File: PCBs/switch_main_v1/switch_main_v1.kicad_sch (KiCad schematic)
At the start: 0 parts

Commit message: Schematic progress
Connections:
- no-connect marks 0 -> 1
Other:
- sheet MCU ports: added ETH_PPS_OUT, MCO1, RMII, SMI; removed none
- sheet PHY 1 ports: added CLK_IN, CLK_OUT, ETHERNET, RGMII, SMI; removed none
- sheet PHY 2 ports: added CLK_IN, CLK_OUT, ETHERNET, RGMII, SMI; removed none
- sheet PHY 3 ports: added CLK_IN, CLK_OUT, ETHERNET, RGMII, SMI; removed none
- sheet PHY 4 ports: added CLK_IN, CLK_OUT, ETHERNET, RGMII, SMI; removed none
- sheet RJ45s ports: added ETHERNET_1, ETHERNET_2, ETHERNET_3, ETHERNET_4; removed none
- sheet Switch ports: added CLK_IN, CLK_OUT, PTP_CLK, RGMII_0, RGMII_1, RGMII_2, RGMII_3, RMII, RST, SPI; removed none
- note added: "Circuits & ICs"
- note added: "Interfaces"
- note added: "Power"
- note added: "Processing"

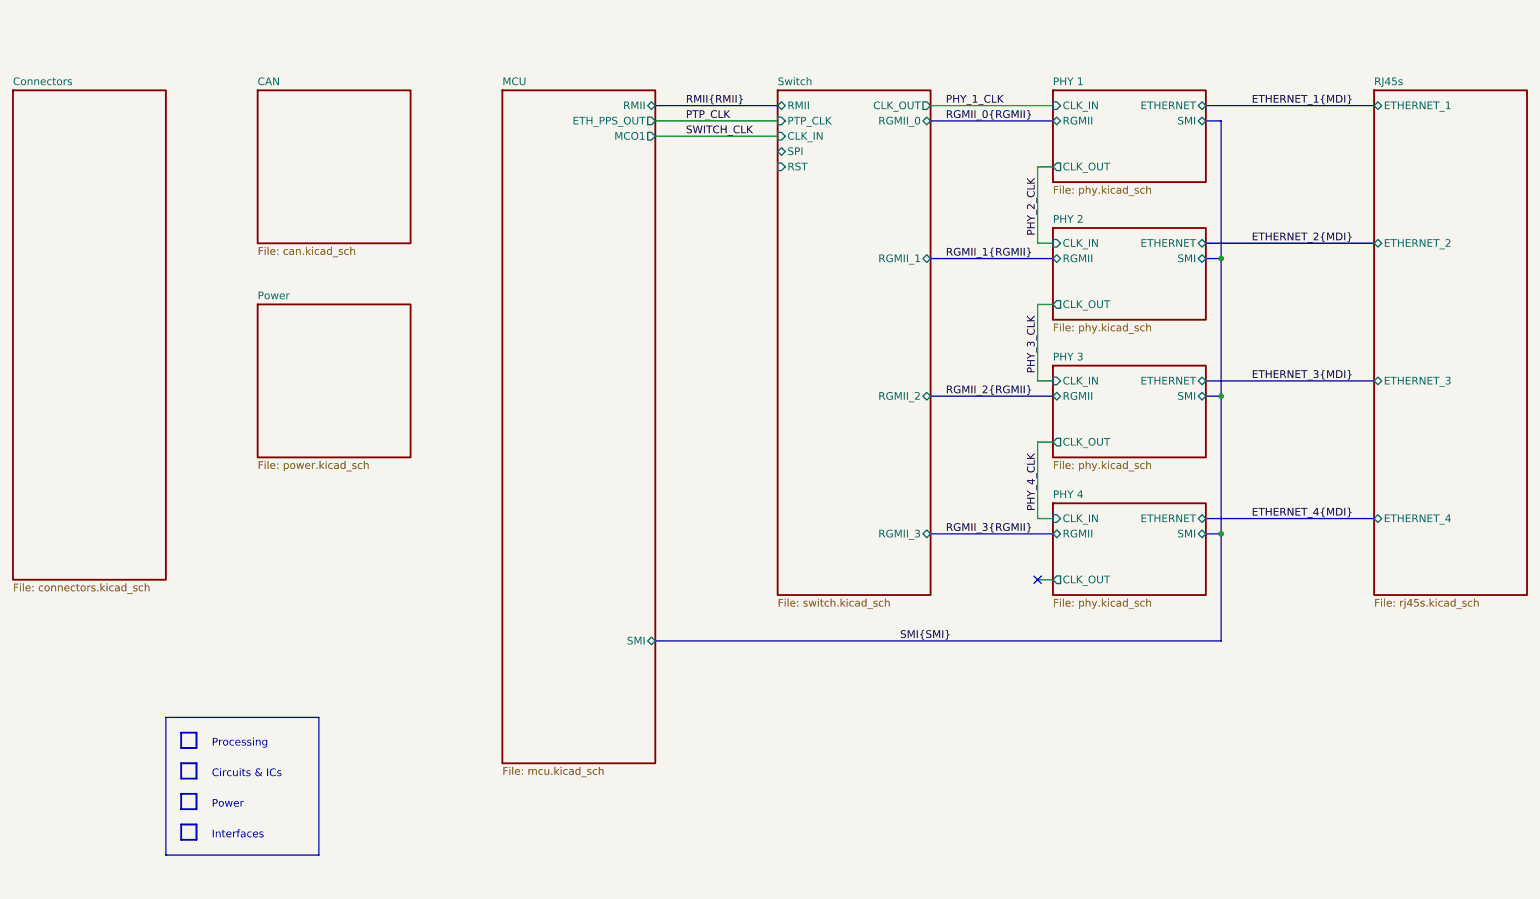
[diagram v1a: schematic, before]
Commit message: Block diagram layout change
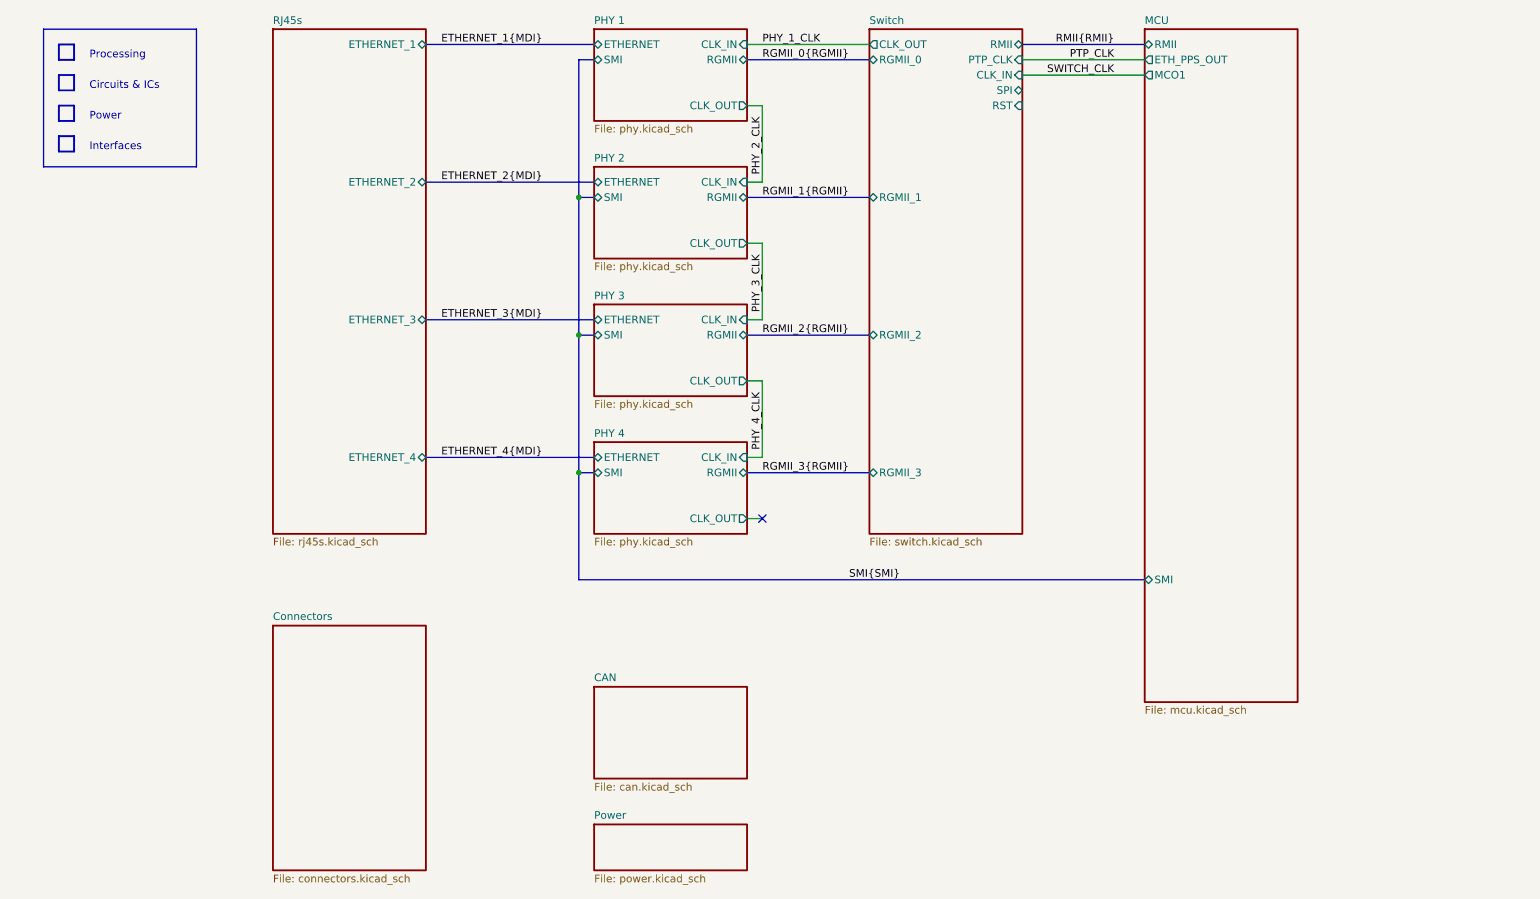
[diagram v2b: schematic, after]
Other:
- company: (none) -> Ben Smith
- title: (none) -> GbE TSN Switch Block Diagram

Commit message: GbE part of schematic done
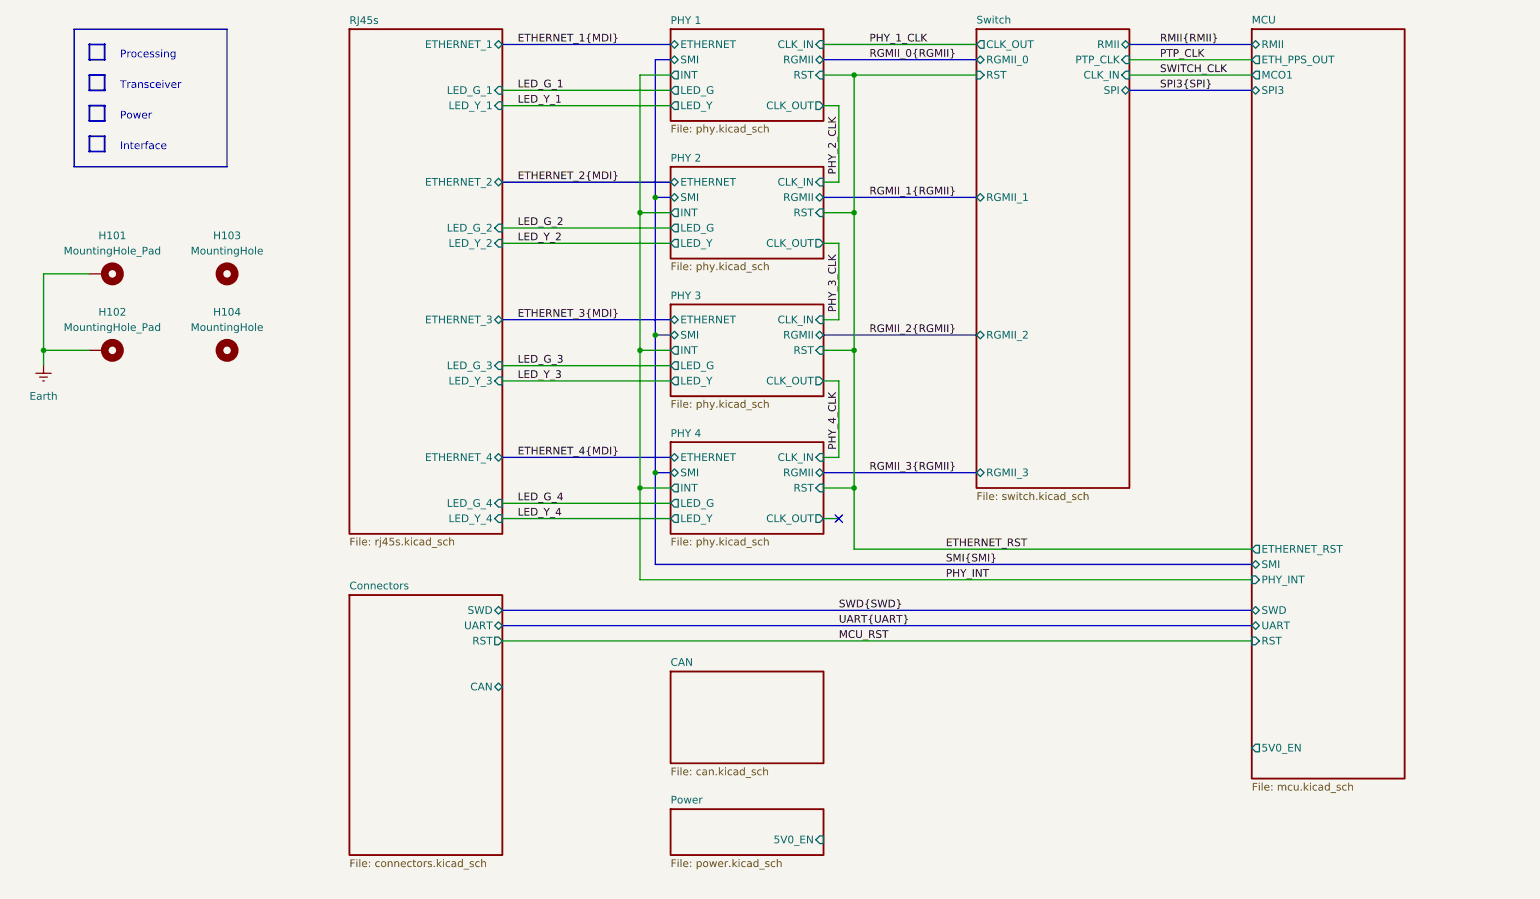
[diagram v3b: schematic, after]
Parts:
- added H101, H102: MountingHole_Pad, MountingHole:MountingHole_3.2mm_M3_DIN965_Pad_TopBottom, symbol Mechanical:MountingHole_Pad
- added H103, H104: MountingHole, MountingHole:MountingHole_3.2mm_M3_DIN965, symbol Mechanical:MountingHole
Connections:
- new net Earth: H101.1, H102.1
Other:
- sheet Connectors ports: added CAN, RST, SWD, UART; removed none
- sheet MCU ports: added 5V0_EN, ETHERNET_RST, PHY_INT, RST, SPI3, SWD, UART; removed none
- sheet PHY 1 ports: added INT, LED_G, LED_Y, RST; removed none
- sheet PHY 2 ports: added INT, LED_G, LED_Y, RST; removed none
- sheet PHY 3 ports: added INT, LED_G, LED_Y, RST; removed none
- sheet PHY 4 ports: added INT, LED_G, LED_Y, RST; removed none
- sheet Power ports: added 5V0_EN; removed none
- sheet RJ45s ports: added LED_G_1, LED_G_2, LED_G_3, LED_G_4, LED_Y_1, LED_Y_2, LED_Y_3, LED_Y_4; removed none
- note added: "Interface"
- note added: "Transceiver"
- note removed: "Circuits & ICs"
- note removed: "Interfaces"

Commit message: Progress on CAN schematic sheet
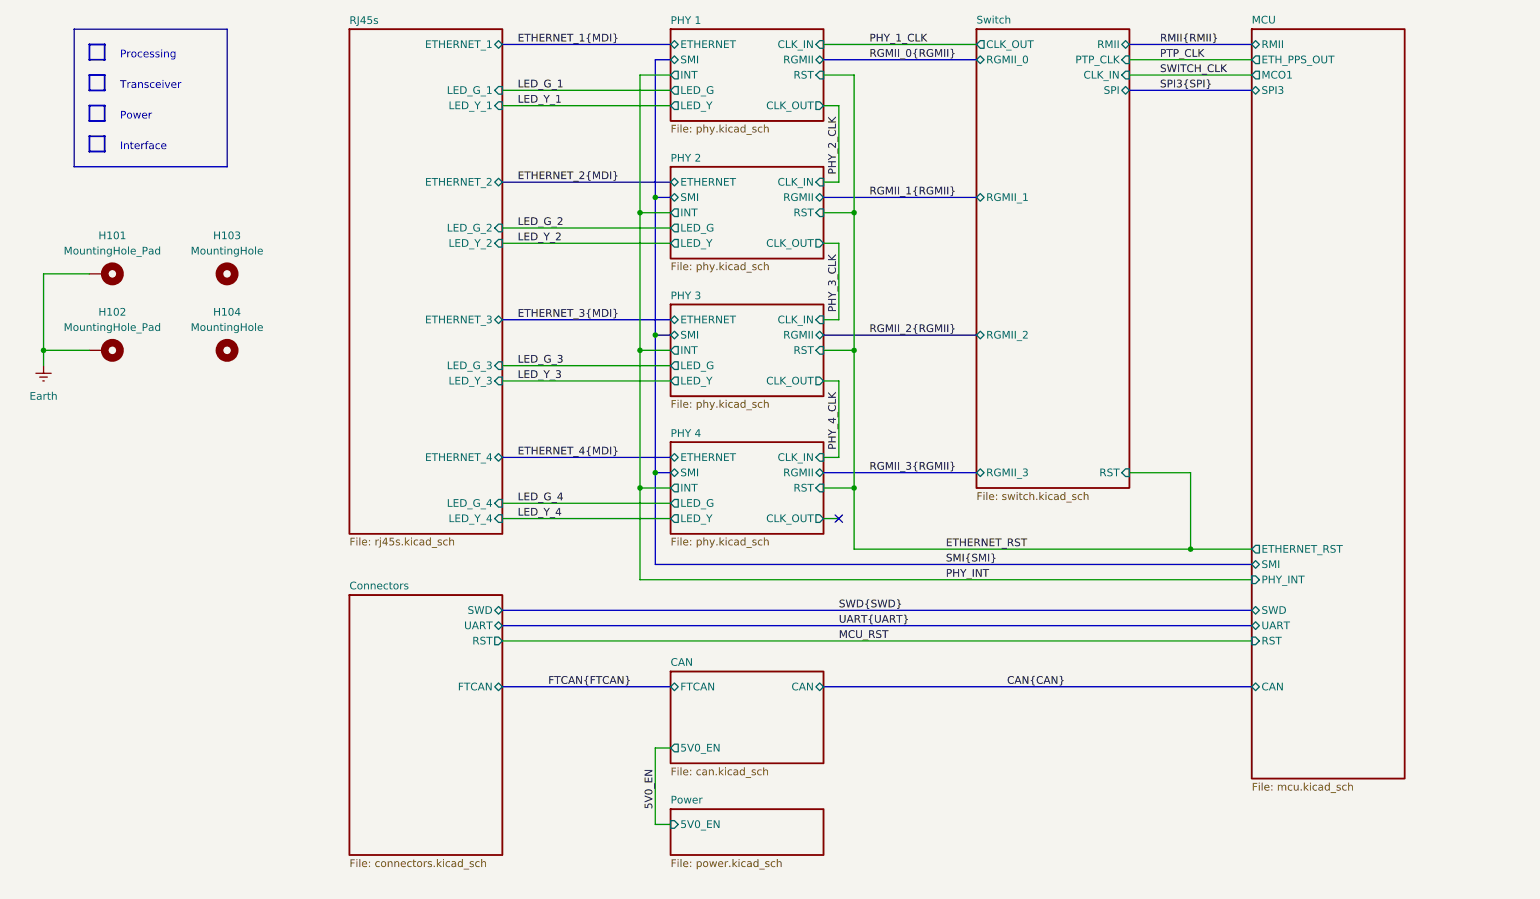
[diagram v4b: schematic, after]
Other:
- sheet CAN ports: added 5V0_EN, CAN, FTCAN; removed none
- sheet Connectors ports: added FTCAN; removed CAN
- sheet MCU ports: added CAN; removed 5V0_EN
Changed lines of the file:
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@@
+	)
+	(junction
+		(at 218.44 114.3)
+		(diameter 0)
+		(color 0 0 0 0)
 	)
 	(junction
@@
 	)
 	(junction
-		(at 162.56 35.56)
-		(diameter 0)
-		(color 0 0 0 0)
-	)
-	(junction
 		(at 162.56 104.14)
 		(diameter 0)
@@
 	(wire
 		(pts
+			(xy 218.44 114.3) (xy 162.56 114.3)
+		)
+		(stroke
+			(width 0)
+			(type default)
+		)
+	)
+	(wire
+		(pts
 			(xy 160.02 99.06) (xy 157.48 99.06)
 		)
@@
 	(bus
 		(pts
+			(xy 104.14 137.16) (xy 132.08 137.16)
+		)
+		(stroke
+			(width 0)
+			(type default)
+		)
+	)
+	(bus
+		(pts
 			(xy 104.14 53.34) (xy 132.08 53.34)
 		)
@@
 	(wire
 		(pts
+			(xy 129.54 147.32) (xy 129.54 160.02)
+		)
+		(stroke
+			(width 0)
+			(type default)
+		)
+	)
+	(wire
+		(pts
 			(xy 104.14 109.22) (xy 132.08 109.22)
 		)
@@
 	(wire
 		(pts
-			(xy 228.6 114.3) (xy 162.56 114.3)
+			(xy 228.6 114.3) (xy 218.44 114.3)
 		)
 		(stroke
@@
 	(wire
 		(pts
+			(xy 208.28 101.6) (xy 218.44 101.6)
+		)
+		(stroke
+			(width 0)
+			(type default)
+		)
+	)
+	(wire
+		(pts
 			(xy 127 104.14) (xy 127 81.28)
 		)
@@
 	(wire
 		(pts
+			(xy 132.08 160.02) (xy 129.54 160.02)
+		)
+		(stroke
+			(width 0)
+			(type default)
+		)
+	)
+	(wire
+		(pts
 			(xy 160.02 76.2) (xy 157.48 76.2)
 		)
@@
 		)
 	)
+	(bus
+		(pts
+			(xy 157.48 137.16) (xy 228.6 137.16)
+		)
+		(stroke
+			(width 0)
+			(type default)
+		)
+	)
 	(wire
 		(pts
@@
 	(wire
 		(pts
-			(xy 162.56 35.56) (xy 182.88 35.56)
+			(xy 129.54 147.32) (xy 132.08 147.32)
 		)
 		(stroke
@@
 		(pts
 			(xy 157.48 81.28) (xy 162.56 81.28)
+		)
+		(stroke
+			(width 0)
+			(type default)
+		)
+	)
+	(wire
+		(pts
+			(xy 218.44 101.6) (xy 218.44 114.3)
 		)
 		(stroke
@@
 		)
 	)
+	(label "CAN{CAN}"
+		(at 187.96 137.16 0)
+		(fields_autoplaced yes)
+		(effects
+			(font
+				(size 1.27 1.27)
+			)
+			(justify left bottom)
+		)
+	)
 	(label "LED_Y_3"
 		(at 106.68 86.36 0)
@@
 		)
 	)
+	(label "FTCAN{FTCAN}"
+		(at 111.76 137.16 0)
+		(fields_autoplaced yes)
+		(effects
+			(font
+				(size 1.27 1.27)
+			)
+			(justify left bottom)
+		)
+	)
 	(label "SWITCH_CLK"
 		(at 213.36 35.56 0)
@@
 	(label "LED_Y_2"
 		(at 106.68 63.5 0)
+		(fields_autoplaced yes)
+		(effects
+			(font
+				(size 1.27 1.27)
+			)
+			(justify left bottom)
+		)
+	)
+	(label "5V0_EN"
+		(at 129.54 157.48 90)
 		(fields_autoplaced yes)
 		(effects
@@
 		)
 		(pin "RST" input
-			(at 182.88 35.56 180)
-			(effects
-				(font
-					(size 1.27 1.27)
-				)
-				(justify left)
+			(at 208.28 101.6 0)
+			(effects
+				(font
+					(size 1.27 1.27)
+				)
+				(justify right)
 			)
 		)
@@
 			)
 		)
+		(pin "5V0_EN" output
+			(at 132.08 147.32 180)
+			(effects
+				(font
+					(size 1.27 1.27)
+				)
+				(justify left)
+			)
+		)
+		(pin "CAN" bidirectional
+			(at 157.48 137.16 0)
+			(effects
+				(font
+					(size 1.27 1.27)
+				)
+				(justify right)
+			)
+		)
+		(pin "FTCAN" bidirectional
+			(at 132.08 137.16 180)
+			(effects
+				(font
+					(size 1.27 1.27)
+				)
+				(justify left)
+			)
+		)
 		(instances
 			(project "switch_main_v1"
@@
 			)
 		)
-		(pin "CAN" bidirectional
-			(at 104.14 137.16 0)
-			(effects
-				(font
-					(size 1.27 1.27)
-				)
-				(justify right)
-			)
-		)
 		(pin "UART" bidirectional
 			(at 104.14 127 0)
@@
 		(pin "RST" output
 			(at 104.14 129.54 0)
+			(effects
+				(font
+					(size 1.27 1.27)
+				)
+				(justify right)
+			)
+		)
+		(pin "FTCAN" bidirectional
+			(at 104.14 137.16 0)
 			(effects
 				(font
@@
 			)
 		)
-		(pin "5V0_EN" output
-			(at 228.6 147.32 180)
-			(effects
-				(font
-					(size 1.27 1.27)
-				)
-				(justify left)
-			)
-		)
 		(pin "ETHERNET_RST" output
 			(at 228.6 114.3 180)
@@
 		(pin "SWD" bidirectional
 			(at 228.6 124.46 180)
+			(effects
+				(font
+					(size 1.27 1.27)
+				)
+				(justify left)
+			)
+		)
+		(pin "CAN" bidirectional
+			(at 228.6 137.16 180)
 			(effects
 				(font
@@
 		)
 		(pin "5V0_EN" input
-			(at 157.48 162.56 0)
-			(effects
-				(font
-					(size 1.27 1.27)
-				)
-				(justify right)
-			)
-		)
+			(at 132.08 160.02 180)
+			(effects
+				(font
+					(size 1.27 1.27)
+				)
+				(justify left)
+			)
+		)

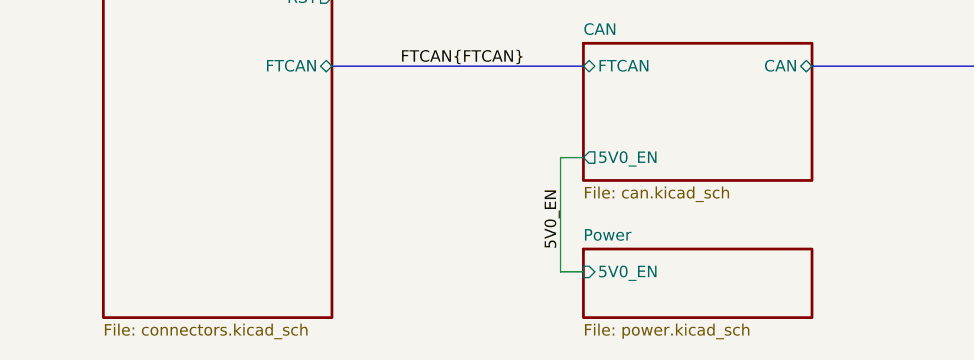
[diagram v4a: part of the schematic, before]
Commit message: Changed MCU to STM32H573VIT3Q
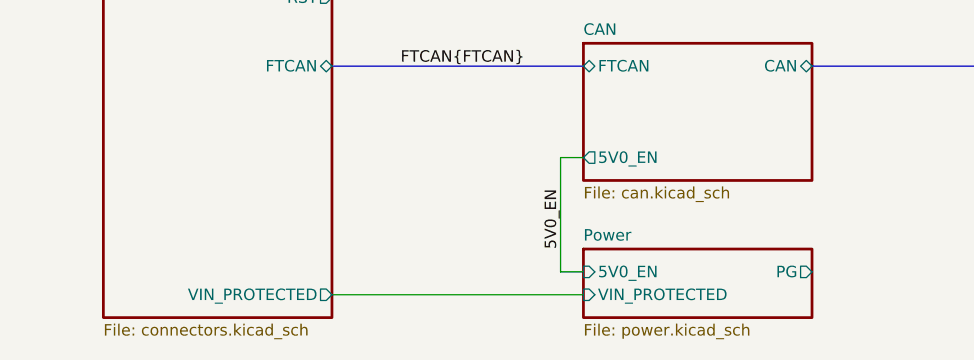
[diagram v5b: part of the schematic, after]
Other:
- sheet Connectors ports: added VIN_PROTECTED; removed none
- sheet Power ports: added PG, VIN_PROTECTED; removed none
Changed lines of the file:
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@@
+	(wire
+		(pts
+			(xy 104.14 162.56) (xy 132.08 162.56)
+		)
+		(stroke
+			(width 0)
+			(type default)
+		)
+	)
 	(wire
 		(pts
@@
 			)
 		)
+		(pin "VIN_PROTECTED" output
+			(at 104.14 162.56 0)
+			(effects
+				(font
+					(size 1.27 1.27)
+				)
+				(justify right)
+			)
+		)
 		(instances
 			(project "switch_main_v1"
@@
 			)
 		)
+		(pin "VIN_PROTECTED" input
+			(at 132.08 162.56 180)
+			(effects
+				(font
+					(size 1.27 1.27)
+				)
+				(justify left)
+			)
+		)
+		(pin "PG" output
+			(at 157.48 160.02 0)
+			(effects
+				(font
+					(size 1.27 1.27)
+				)
+				(justify right)
+			)
+		)
